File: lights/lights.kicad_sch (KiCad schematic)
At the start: 16 parts, among them J1 Barrel_Jack_Switch, J2 Screw_Terminal_01x06, J3 Screw_Terminal_01x05, U1 L7805

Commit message: Version 2022.09.19 - Added Raspberry Pi & Mega
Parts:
- removed J1: Barrel_Jack_Switch, Connector_BarrelJack:BarrelJack_Horizontal, symbol Connector:Barrel_Jack_Switch
- removed J2: Screw_Terminal_01x06, TerminalBlock:TerminalBlock_bornier-6_P5.08mm, symbol Connector:Screw_Terminal_01x06
- removed J3: Screw_Terminal_01x05, symbol Connector:Screw_Terminal_01x05
- added J?: Screw_Terminal_01x06, symbol Connector:Screw_Terminal_01x06
- added J?: Screw_Terminal_01x02, symbol Connector:Screw_Terminal_01x02
- added J?: Screw_Terminal_01x05, symbol Connector:Screw_Terminal_01x05
- C?: renamed from C2; value 0.1uF -> C_Polarized
- C?: renamed from C3; value 0.1uF -> C_Polarized
- C?: renamed from C1; value 0.33uF -> C_Polarized
- R?: renamed from R1; value 330Ω -> R
- TP?: renamed from TP1; footprint (none) -> TestPoint:TestPoint_Pad_D1.5mm
- renumbered D2 to D?, D1 to D?, U1 to U?
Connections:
- net +12V: now also J?.2 (Pin_2)
- net DC+: now also J?.1 (Pin_1)
- net DC-: now also J?.2 (Pin_2)
- net GND: now also J?.1 (Pin_1)
- net IN1: now also J?.3 (Pin_3), J?.5 (Pin_5)
- net IN2: now also J?.4 (Pin_4), J?.4 (Pin_4)
- net IN3: now also J?.3 (Pin_3), J?.5 (Pin_5)
- net IN4: now also J?.2 (Pin_2), J?.6 (Pin_6)
- net at C?.1: now also J?.1 (Pin_1)

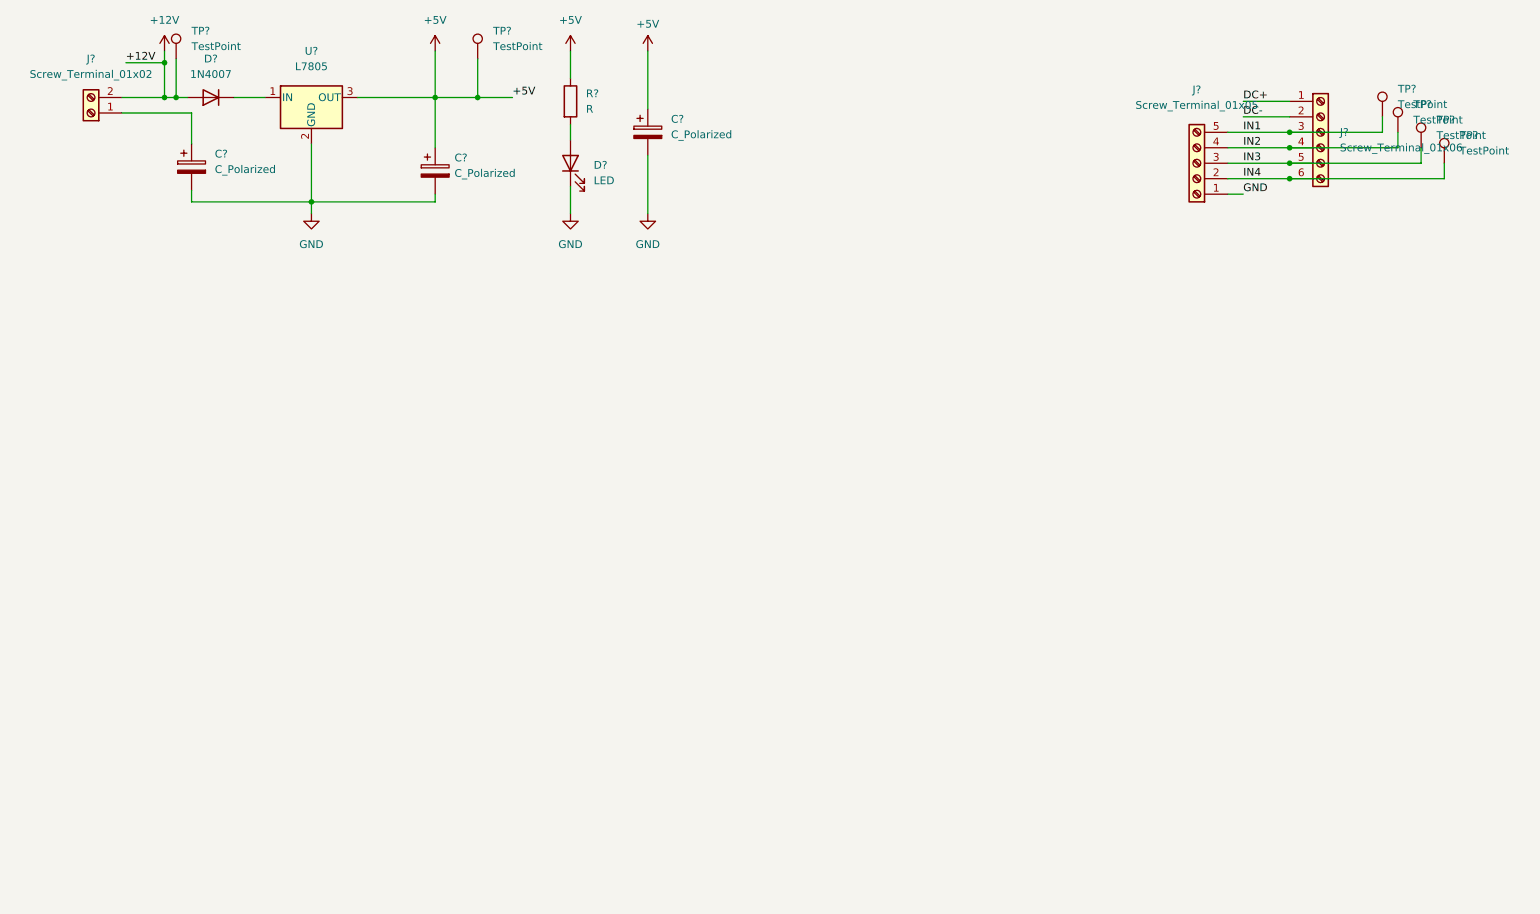
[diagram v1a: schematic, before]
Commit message: Version 2022.09.20 - Added Terminal Blocks
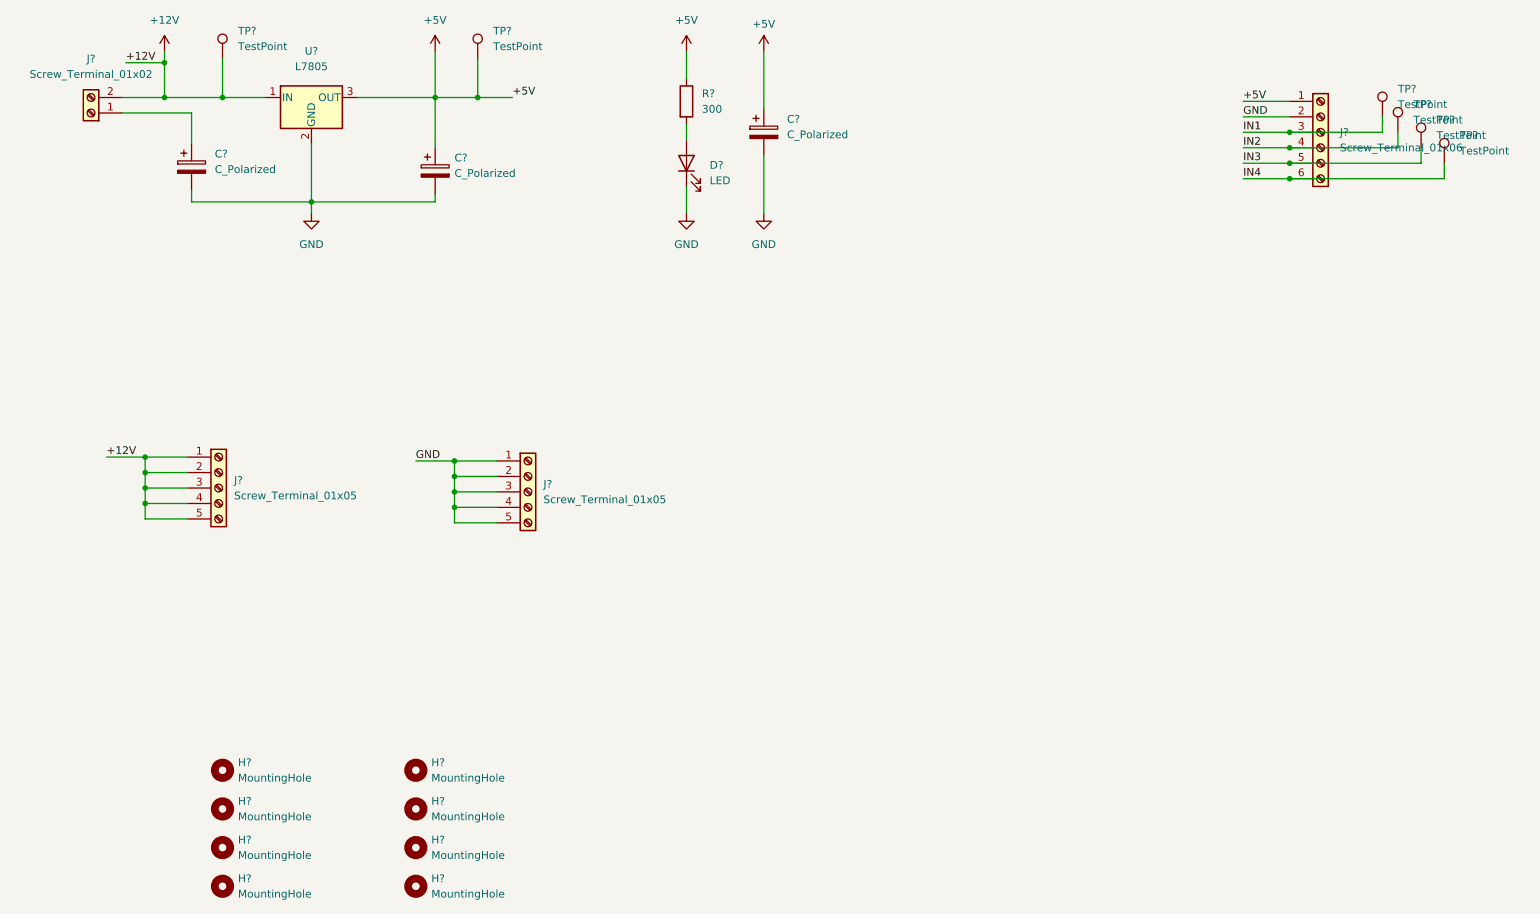
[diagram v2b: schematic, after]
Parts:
- removed D?: 1N4007, Diode_THT:D_DO-41_SOD81_P10.16mm_Horizontal, symbol Diode:1N4007
- removed J?: Screw_Terminal_01x05, symbol Connector:Screw_Terminal_01x05
- added H? (x7): MountingHole, symbol Mechanical:MountingHole
- added H?: MountingHole, MountingHole:MountingHole_3.2mm_M3, symbol Mechanical:MountingHole
- added J? (x2): Screw_Terminal_01x05, symbol Connector:Screw_Terminal_01x05
- R?: value R -> 300
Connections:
- net DC+ is gone; now on net +5V: J?.1 (Pin_1)
- net DC- is gone; now on net GND: J?.2 (Pin_2)
- net +12V: now also U?.1 (IN), J?.1 (Pin_1), J?.2 (Pin_2), J?.3 (Pin_3), J?.4 (Pin_4), J?.5 (Pin_5)
- net GND: now also J?.1 (Pin_1), J?.2 (Pin_2), J?.3 (Pin_3), J?.4 (Pin_4), J?.5 (Pin_5)
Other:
- moved on the sheet: C?, D?, R?, TP?
